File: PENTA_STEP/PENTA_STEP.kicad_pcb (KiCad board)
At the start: 4 copper layers, 200 x 100 mm, 331 parts, among them J1 DB25_Female_LCNC, J10 ENC_HEADER, J11 ENC_HEADER, J12 PSoC_PROG, J13 PWR_SW_CH1, J14 SCREW TERM, J15 SCREW TERM, J16 ENC_HEADER, J17 ENC_HEADER, J18 SCREW TERM, J19 SCREW TERM, J2 MTA-100, J20 CYP_I2C, J21 PWR_SW_CH2, J3 USB_B, J4 SPARE_IN, J5 ENC_HEADER, J7 CYP_GPIO, J9 SCREW TERM, Q1 BUK9K45-100E,115, Q10 BUK9K45-100E,115, Q11 BUK9K45-100E,115, Q12 BUK9K45-100E,115, Q13 BUK9K45-100E,115, Q14 BUK9K45-100E,115, Q15 BUK9K45-100E,115, Q16 BUK9K45-100E,115, Q17 BUK9K45-100E,115, Q18 BUK9K45-100E,115, Q19 BUK9K45-100E,115, Q2 BUK9K45-100E,115, Q20 BUK9K45-100E,115, Q21 AON7804, Q3 BUK9K45-100E,115, Q4 BUK9K45-100E,115, Q5 BUK9K45-100E,115, Q6 BUK9K45-100E,115, Q7 BUK9K45-100E,115, Q8 BUK9K45-100E,115, Q9 BUK9K45-100E,115, U2 CY8C5468AXI-LP106, U3 TMC5160-TA, U4 TMC5160-TA, U5 TMC5160-TA, U6 TMC5160-TA, U7 TMC5160-TA

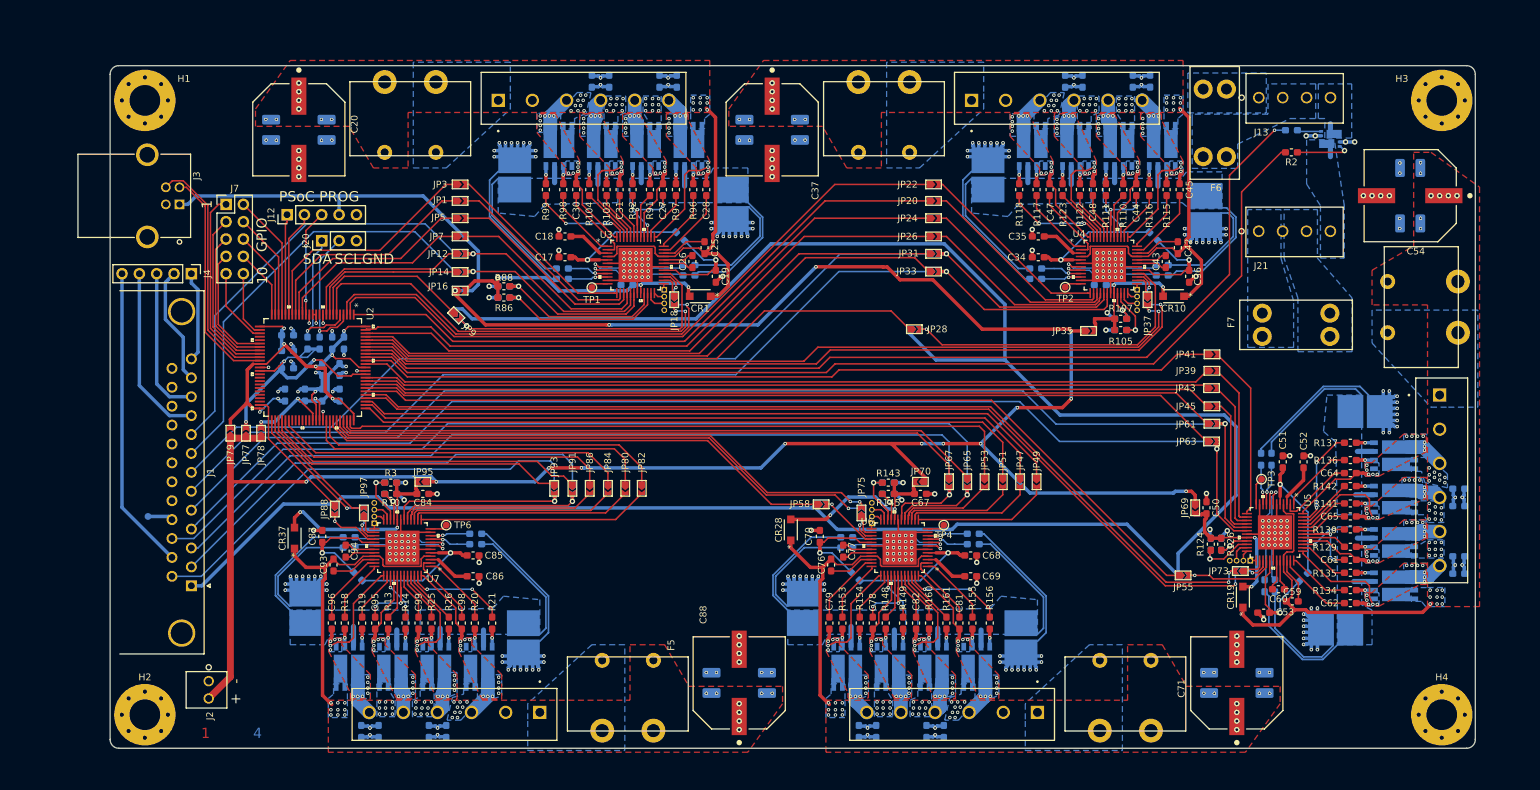
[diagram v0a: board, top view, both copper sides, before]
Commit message: finished layout, added top and bottom layer ground pours, added fuses for FET outputs, but forgot to save ;)
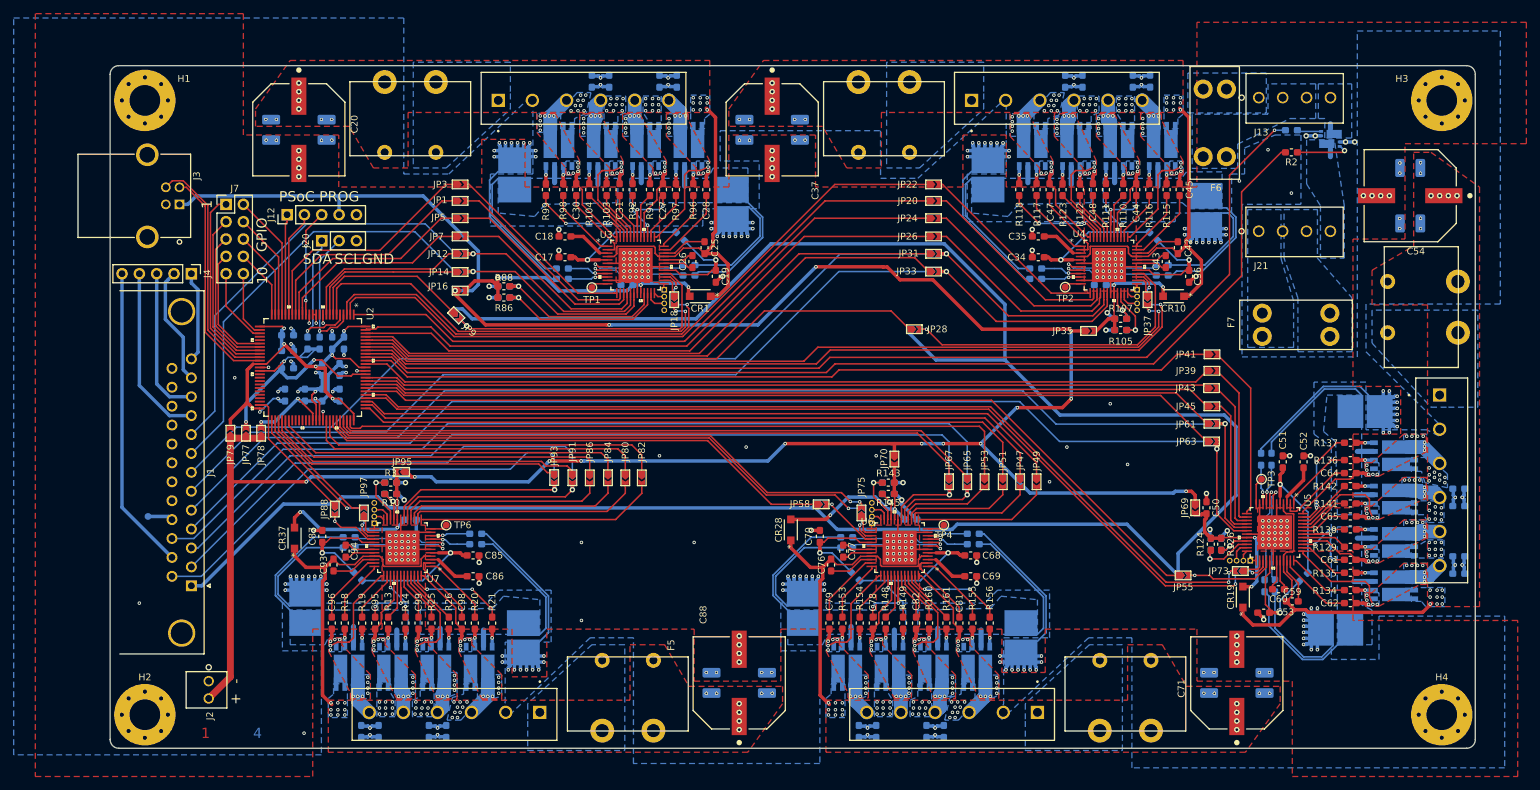
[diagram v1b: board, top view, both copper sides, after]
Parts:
- C67, C84: moved to B.Cu
- moved JP70 5.06 mm to (160.6, 107.2), turned to 270 degrees
- moved C84 4.20 mm to (89.7, 116.1)
- moved C67 4.00 mm to (163.0, 116.0)
- moved JP95 3.42 mm to (88.4, 109.0)
- moved JP93 1.57 mm to (110.8, 109.9)
- moved JP94 1.57 mm to (110.8, 109.9)
- moved JP91 1.55 mm to (113.4, 109.9)
- moved JP92 1.55 mm to (113.4, 109.9)
- moved JP84 1.55 mm to (118.7, 109.9)
- moved JP80 1.53 mm to (121.2, 109.9)
- moved JP82 1.53 mm to (123.6, 109.9)
- moved JP86 1.53 mm to (116.0, 109.9)
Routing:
- net /VCC_CONT: track 388.5 -> 382.6 mm
- net GND: track 413.6 -> 417.4 mm, vias 321 -> 335
- net /DRIVE_5/VCC_IO: track 29.7 -> 27.8 mm
- net /DRIVE_5/MISO: track 28.3 -> 30.1 mm
- net /DRIVE_5/SCK: track 32.4 -> 34.0 mm
- net /DRIVE_5/MOSI: track 30.5 -> 32.1 mm
- net /DRIVE_5/CS: track 33.9 -> 35.5 mm
- net /DRIVE_2/REFL_STEP: track 30.0 -> 31.5 mm
- net /DRIVE_2/REFR_DIR: track 30.3 -> 31.7 mm
- net /DRIVE_2/VCC_IO: track 21.7 -> 20.5 mm
- net /CYP_SCK5: track 51.4 -> 50.1 mm
- net /DRIVE_2/MISO: track 29.1 -> 30.1 mm
- net /CYP_MISO5: track 50.3 -> 49.6 mm
- net /DRIVE_5/REFL_STEP: track 28.1 -> 28.8 mm
- net /CYP_DIR5: track 44.7 -> 44.1 mm
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- added copper zone on B.Cu, net GND
- added copper zone on F.Cu, net GND

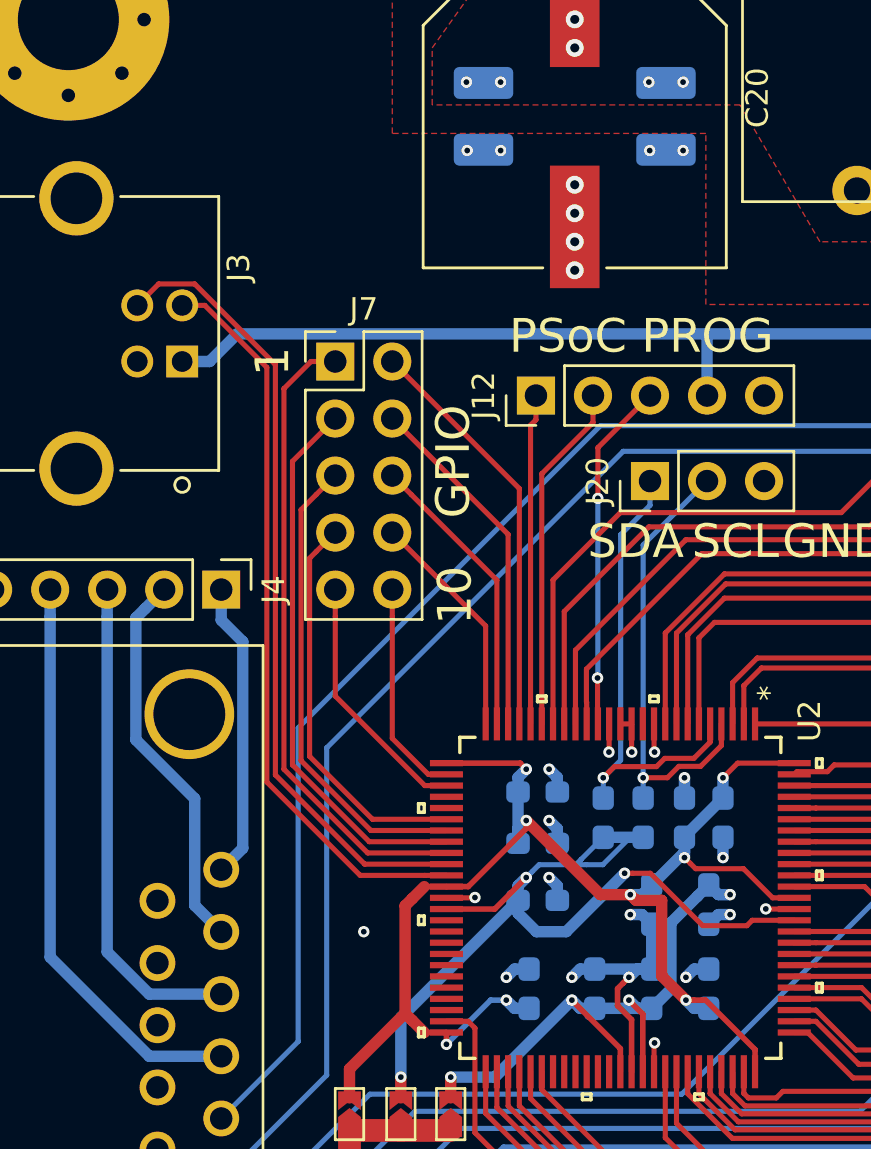
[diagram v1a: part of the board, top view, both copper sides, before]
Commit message: finalized BOM, found TMC5160-TA being replaced by TMC5160A-TA
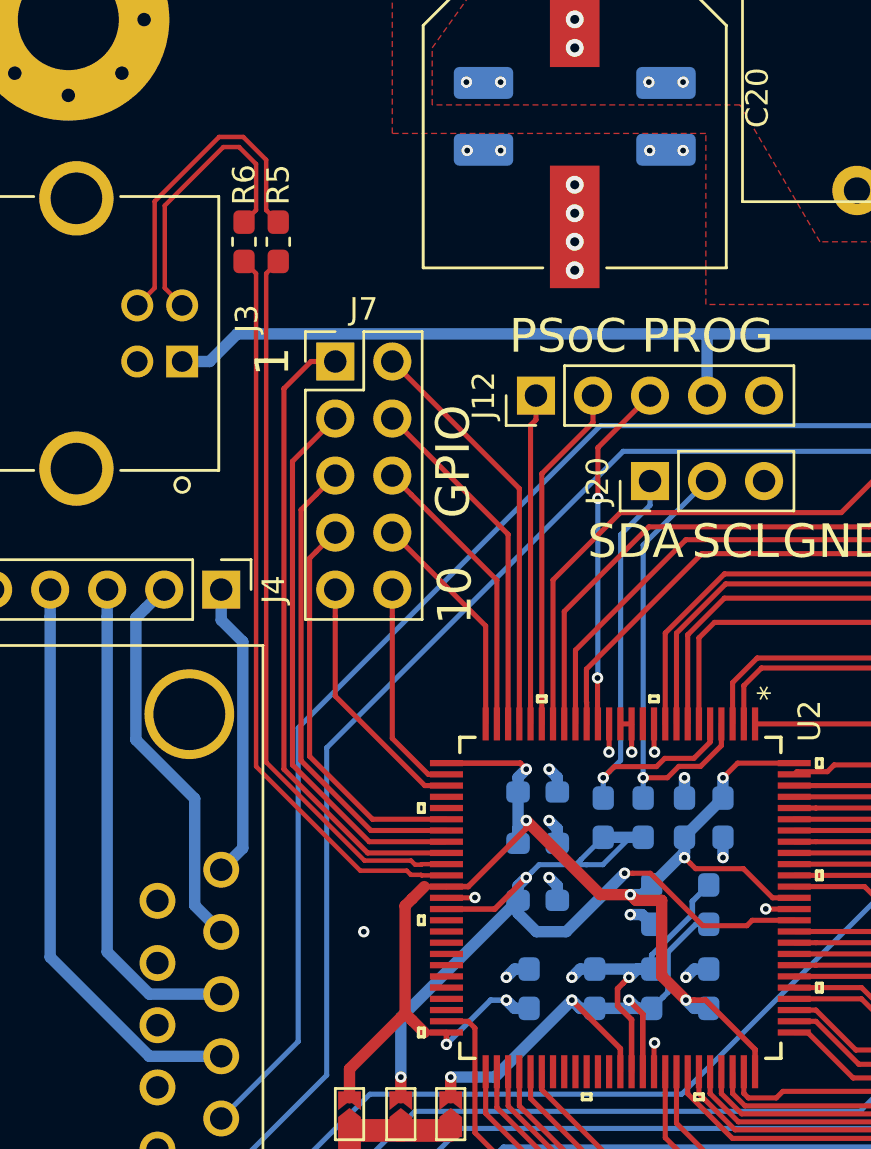
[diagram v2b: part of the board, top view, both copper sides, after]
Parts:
- added R5: 22R, Resistor_SMD:R_0603_1608Metric_Pad1.05x0.95mm_HandSolder, F.Cu at (60.2, 64.5)
- added R6: 22R, Resistor_SMD:R_0603_1608Metric_Pad1.05x0.95mm_HandSolder, F.Cu at (58.6, 64.5)
- turned C4 to 90 degrees
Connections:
- C4 pad 2: GND -> GNDA
- C6 pad 2: GNDA -> GND
- J3 pad 2: /USBIO_D- -> /D-
- J3 pad 3: /USBIO_D+ -> /D+
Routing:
- net /D+: track 0.00 -> 14.5 mm
- net /D-: track 0.00 -> 13.0 mm
- net /USBIO_D+: track 35.6 -> 32.5 mm
- net /VDDA: track 27.8 -> 25.3 mm, vias 4 -> 3
- net GNDA: track 12.7 -> 14.3 mm, vias 3 -> 2
